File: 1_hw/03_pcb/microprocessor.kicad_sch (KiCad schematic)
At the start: 29 parts, among them U3 STM32F446ZETx, Y2 32.768k

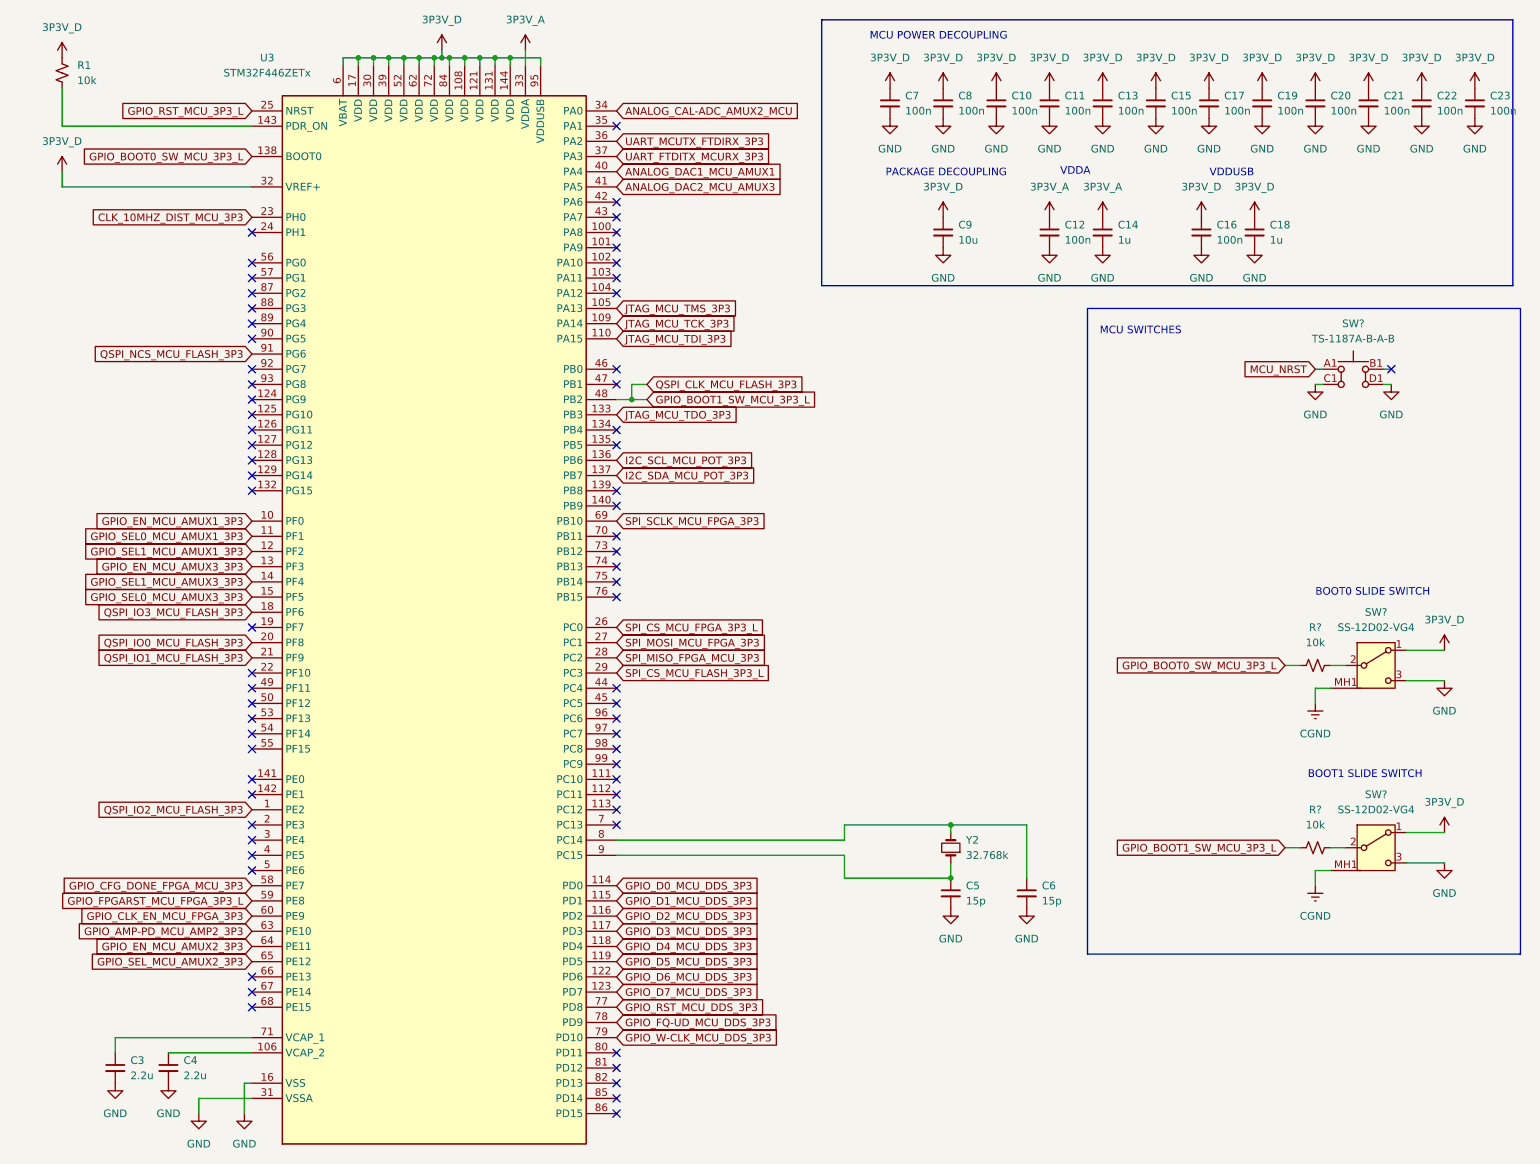
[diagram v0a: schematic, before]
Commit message: FEAT: Added Clocking Sheet, FPGA Flash, and FPGA Decoupling.
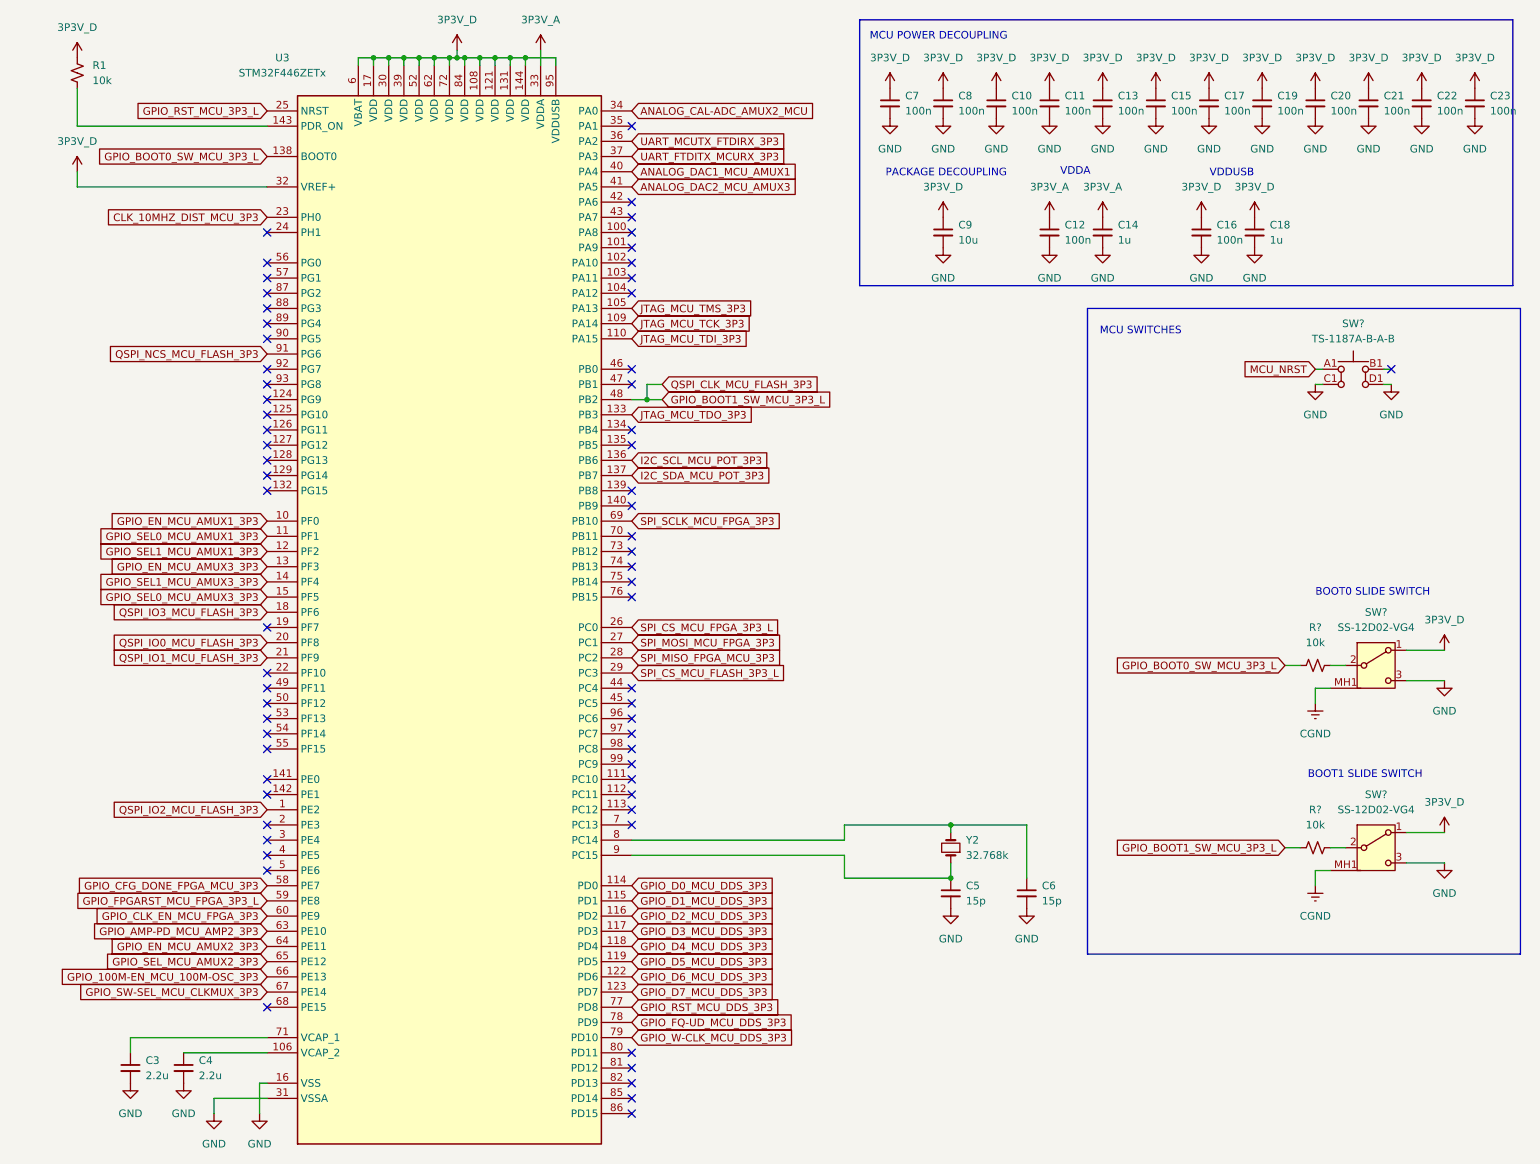
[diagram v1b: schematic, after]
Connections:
- net GPIO_100M-EN_MCU_100M-OSC_3P3: now reaches U3.66 (PE13)
- net GPIO_SW-SEL_MCU_CLKMUX_3P3: now reaches U3.67 (PE14)
- no-connect marks 67 -> 65
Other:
- moved on the sheet: C3, C4, R1, U3

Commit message: FEAT: Added Connectors on Schematic. Created Connector Footprints.
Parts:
- gave numbers to parts that had none: 5
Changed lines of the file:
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@@
 		(on_board yes)
 		(dnp no)
-		(property "Reference" "SW?"
+		(property "Reference" "SW3"
 			(at 236.22 143.51 0)
 			(effects
@@
 			(project "arb"
 				(path "/866ef9be-3b01-4288-a6e0-a2357aa17e50/1173c135-6710-44aa-af07-a45f7e01d96a"
-					(reference "SW?")
+					(reference "SW3")
 					(unit 1)
 				)
@@
 		(dnp no)
 		(fields_autoplaced yes)
-		(property "Reference" "R?"
+		(property "Reference" "R41"
 			(at 226.06 146.05 90)
 			(effects
@@
 			(project "arb"
 				(path "/866ef9be-3b01-4288-a6e0-a2357aa17e50/1173c135-6710-44aa-af07-a45f7e01d96a"
-					(reference "R?")
+					(reference "R41")
 					(unit 1)
 				)
@@
 		(dnp no)
 		(fields_autoplaced yes)
-		(property "Reference" "R?"
+		(property "Reference" "R40"
 			(at 226.06 115.57 90)
 			(effects
@@
 			(project "arb"
 				(path "/866ef9be-3b01-4288-a6e0-a2357aa17e50/1173c135-6710-44aa-af07-a45f7e01d96a"
-					(reference "R?")
+					(reference "R40")
 					(unit 1)
 				)
@@
 		(on_board yes)
 		(dnp no)
-		(property "Reference" "SW?"
+		(property "Reference" "SW2"
 			(at 236.22 113.03 0)
 			(effects
@@
 			(project ""
 				(path "/866ef9be-3b01-4288-a6e0-a2357aa17e50/1173c135-6710-44aa-af07-a45f7e01d96a"
-					(reference "SW?")
+					(reference "SW2")
 					(unit 1)
 				)
@@
 		(dnp no)
 		(fields_autoplaced yes)
-		(property "Reference" "SW?"
+		(property "Reference" "SW1"
 			(at 232.41 64.77 0)
 			(effects
@@
 			(project ""
 				(path "/866ef9be-3b01-4288-a6e0-a2357aa17e50/1173c135-6710-44aa-af07-a45f7e01d96a"
-					(reference "SW?")
-					(unit 1)
-				)
+					(reference "SW1")
+					(unit 1)
+				)

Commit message: FEAT: Assigned Reference Designators; Assigned Passives Part Numbers & Footprints (0603); Assigned LCSC P/Ns.
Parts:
- C38: renamed from C3; LCSC (none) -> C23630; PN FCC0603X225K160CT -> (none); Part Number (none) -> CL10A225KO8NNNC
- C39: renamed from C4; LCSC (none) -> C23630; PN FCC0603X225K160CT -> (none); Part Number (none) -> CL10A225KO8NNNC
- C40: renamed from C7; LCSC (none) -> C24452; PN CL10B104JB8NNNC -> (none); Part Number (none) -> CL10B104JB8NNNC
- C41: renamed from C8; LCSC (none) -> C24452; PN CL10B104JB8NNNC -> (none); Part Number (none) -> CL10B104JB8NNNC
- C42: renamed from C9; LCSC (none) -> C19702; PN FCC0603X106K6R3CT -> (none); Part Number (none) -> CL10A106KP8NNNC
- C43: renamed from C5; LCSC (none) -> C1644; PN CC0603GRNPO9BN150 -> (none); Part Number (none) -> CL10C150JB8NNNC
- C44: renamed from C10; LCSC (none) -> C24452; PN CL10B104JB8NNNC -> (none); Part Number (none) -> CL10B104JB8NNNC
- C45: renamed from C6; LCSC (none) -> C1644; PN CC0603GRNPO9BN150 -> (none); Part Number (none) -> CL10C150JB8NNNC
- C46: renamed from C11; LCSC (none) -> C24452; PN CL10B104JB8NNNC -> (none); Part Number (none) -> CL10B104JB8NNNC
- C47: renamed from C12; LCSC (none) -> C24452; PN CL10B104JB8NNNC -> (none); Part Number (none) -> CL10B104JB8NNNC
- C48: renamed from C13; LCSC (none) -> C24452; PN CL10B104JB8NNNC -> (none); Part Number (none) -> CL10B104JB8NNNC
- C49: renamed from C14; LCSC (none) -> C15849; PN TMK107AB7105KAHT -> (none); Part Number (none) -> CL10A105KB8NNNC
- C50: renamed from C15; LCSC (none) -> C24452; PN CL10B104JB8NNNC -> (none); Part Number (none) -> CL10B104JB8NNNC
- C51: renamed from C16; LCSC (none) -> C24452; PN CL10B104JB8NNNC -> (none); Part Number (none) -> CL10B104JB8NNNC
- C52: renamed from C17; LCSC (none) -> C24452; PN CL10B104JB8NNNC -> (none); Part Number (none) -> CL10B104JB8NNNC
- C53: renamed from C18; LCSC (none) -> C15849; PN TMK107AB7105KAHT -> (none); Part Number (none) -> CL10A105KB8NNNC
- C54: renamed from C19; LCSC (none) -> C24452; PN CL10B104JB8NNNC -> (none); Part Number (none) -> CL10B104JB8NNNC
- C55: renamed from C20; LCSC (none) -> C24452; PN CL10B104JB8NNNC -> (none); Part Number (none) -> CL10B104JB8NNNC
- C56: renamed from C21; LCSC (none) -> C24452; PN CL10B104JB8NNNC -> (none); Part Number (none) -> CL10B104JB8NNNC
- C57: renamed from C22; LCSC (none) -> C24452; PN CL10B104JB8NNNC -> (none); Part Number (none) -> CL10B104JB8NNNC
- C58: renamed from C23; LCSC (none) -> C24452; PN CL10B104JB8NNNC -> (none); Part Number (none) -> CL10B104JB8NNNC
- R30: renamed from R1; LCSC (none) -> C25804; PN CR-03FC7---10K -> (none); Part Number (none) -> 0603WAF1002T5E
- R31: renamed from R40; LCSC (none) -> C25804; PN CR-03FC7---10K -> (none); Part Number (none) -> 0603WAF1002T5E
- R32: renamed from R41; LCSC (none) -> C25804; PN CR-03FC7---10K -> (none); Part Number (none) -> 0603WAF1002T5E
- SW1: footprint BRZK_TBD -> (none); LCSC (none) -> C318884
- SW2, SW3: footprint BRZK_TBD -> (none); LCSC (none) -> C136719
- U11: renamed from U3; LCSC (none) -> C2970508
- Y1: renamed from Y2; LCSC (none) -> C32346; PN Q13FC13500004 -> (none); Part Number (none) -> Q13FC13500004

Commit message: FEAT: Added MCU Flash. Finished creating & assigning footprints. Ran ERC & cleared out issues. Ready for Layout.
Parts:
- SW1: footprint (none) -> BRZK_SW:SW_SPST_BUTTON_TS-1187A-B-A-B
- SW2, SW3: footprint (none) -> BRZK_SW:SW_TH_Slide_SPDT_Straight_SS-12D02-VG4
- renumbered R30 to R31, R31 to R32, R32 to R33
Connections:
- net MCU_NRST is gone; now on net GPIO_RST_MCU_3P3_L: SW1.A1 (COM_1)
- net CGND renamed C_GND

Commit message: FEAT: Finished placement of components, switches, etc.
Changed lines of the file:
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@@
 	(rectangle
 		(start 149.86 13.97)
-		(end 259.08 58.42)
+		(end 261.62 58.42)
 		(stroke
 			(width 0)

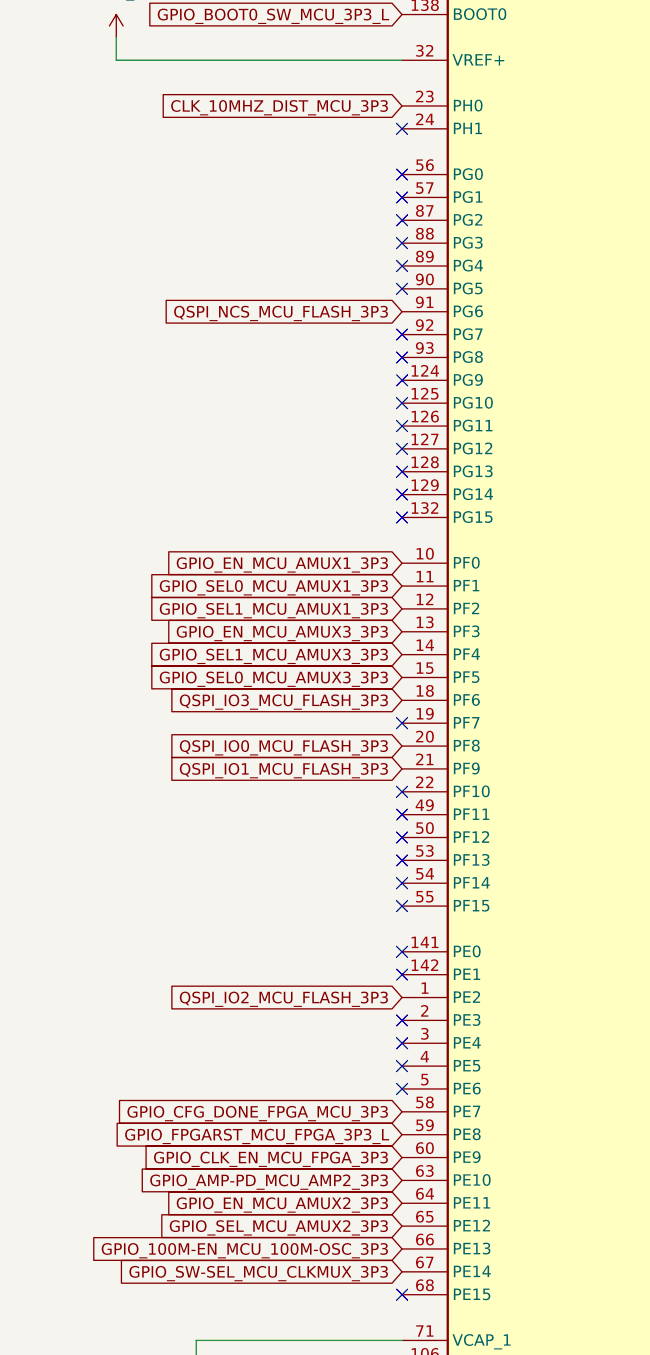
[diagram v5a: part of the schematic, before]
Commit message: FEAT: Laid out MCU DDS. Changed some MCU Pins for better routability.
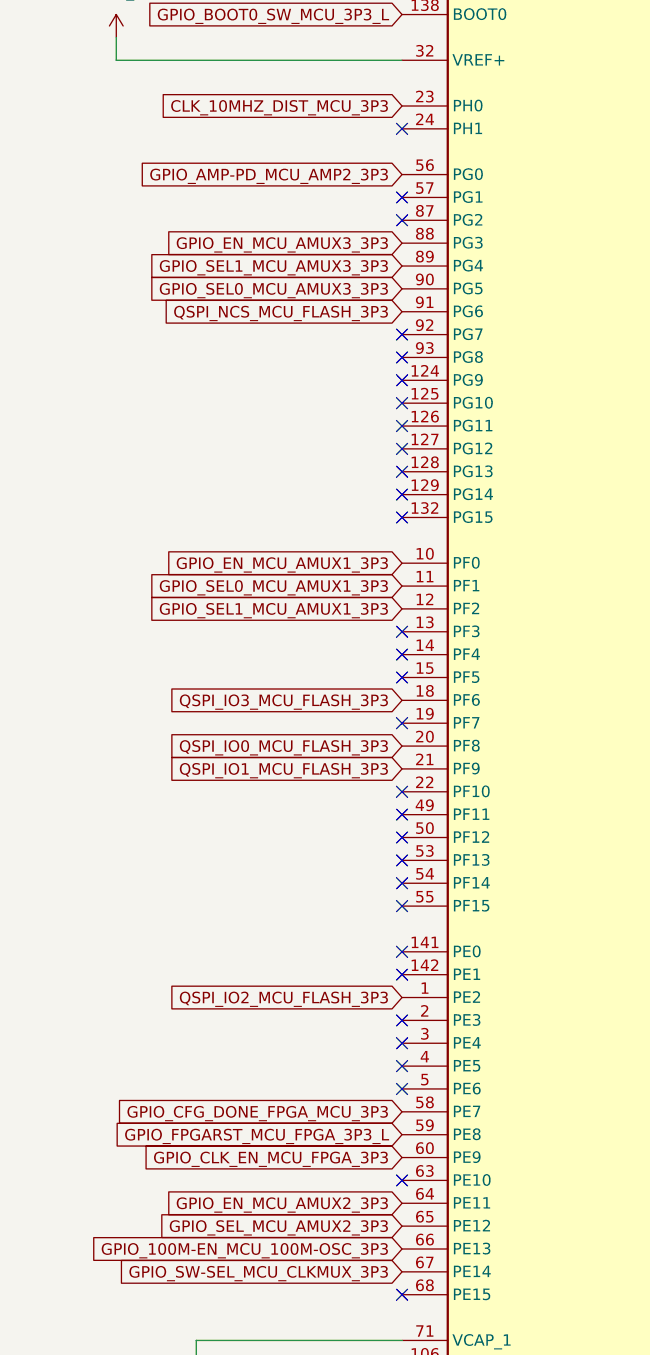
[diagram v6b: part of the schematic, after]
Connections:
- net GPIO_AMP-PD_MCU_AMP2_3P3: now also U11.56 (PG0); no longer U11.63 (PE10)
- net GPIO_EN_MCU_AMUX3_3P3: now also U11.88 (PG3); no longer U11.13 (PF3)
- net GPIO_SEL0_MCU_AMUX3_3P3: now also U11.90 (PG5); no longer U11.15 (PF5)
- net GPIO_SEL1_MCU_AMUX3_3P3: now also U11.89 (PG4); no longer U11.14 (PF4)

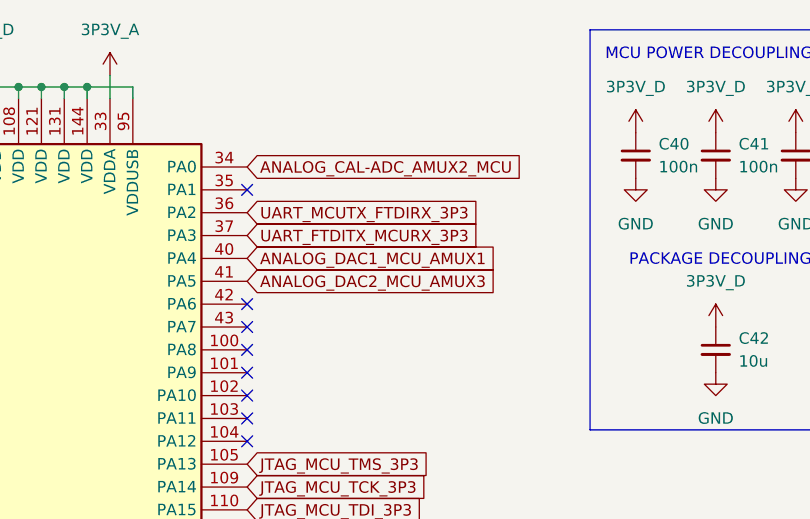
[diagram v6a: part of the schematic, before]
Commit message: MINOR: Layout. 3.3V Analog Power, FTDI IC. Clocks.
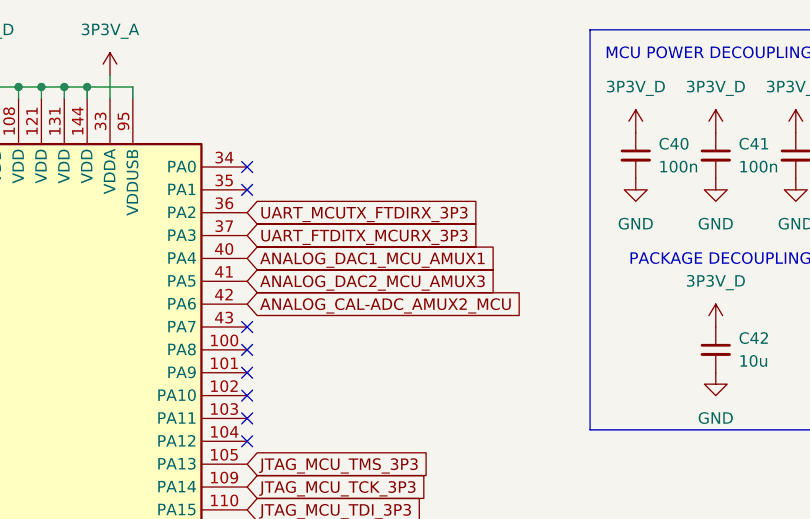
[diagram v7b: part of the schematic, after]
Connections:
- net ANALOG_CAL-ADC_AMUX2_MCU: now also U11.42 (PA6); no longer U11.34 (PA0)

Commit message: MINOR: Layout, I2C Potentiometer, QSPI MCU Memory.
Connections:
- net I2C_SCL_MCU_POT_3P3: now also U11.69 (PB10); no longer U11.136 (PB6)
- net I2C_SDA_MCU_POT_3P3: now also U11.70 (PB11); no longer U11.137 (PB7)
- net SPI_SCLK_MCU_FPGA_3P3: no longer U11.69 (PB10)
- no-connect marks 65 -> 66
